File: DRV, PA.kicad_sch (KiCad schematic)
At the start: 157 parts, among them Q10 2SC5171, Q11 2SA1930, Q12 BD139, Q13 BD139, Q14 IRF630, Q15 IRF630, Q16 IRF630, Q17 IRF630, Q2 2N2222A, Q3 2N2222A, Q4 2N3866, Q5 2N3866, Q6 BD139, Q7 BD139, Q8 2SC5171, Q9 2SA1930

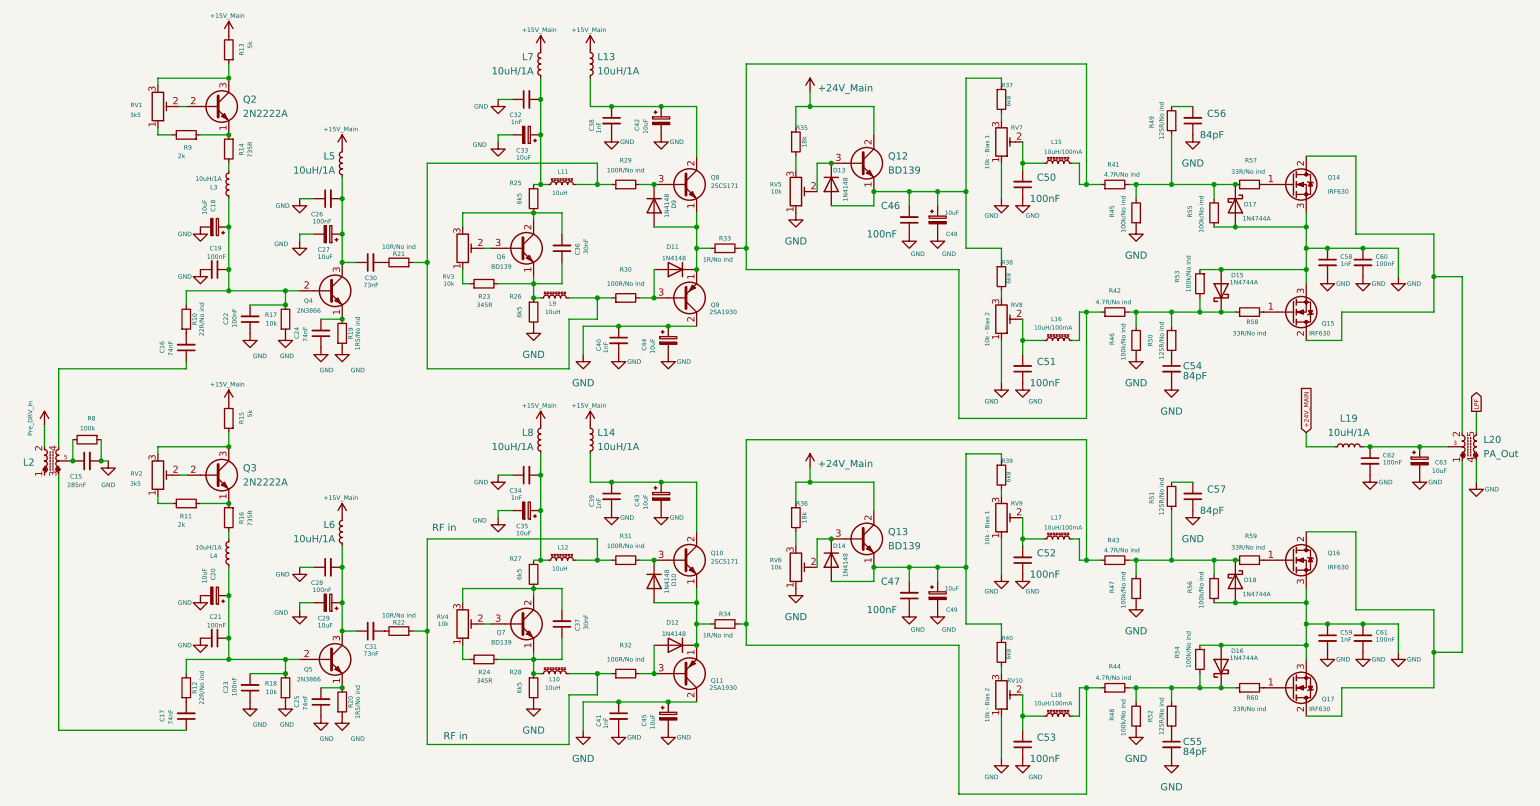
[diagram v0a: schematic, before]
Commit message: Resistive adder of mixers
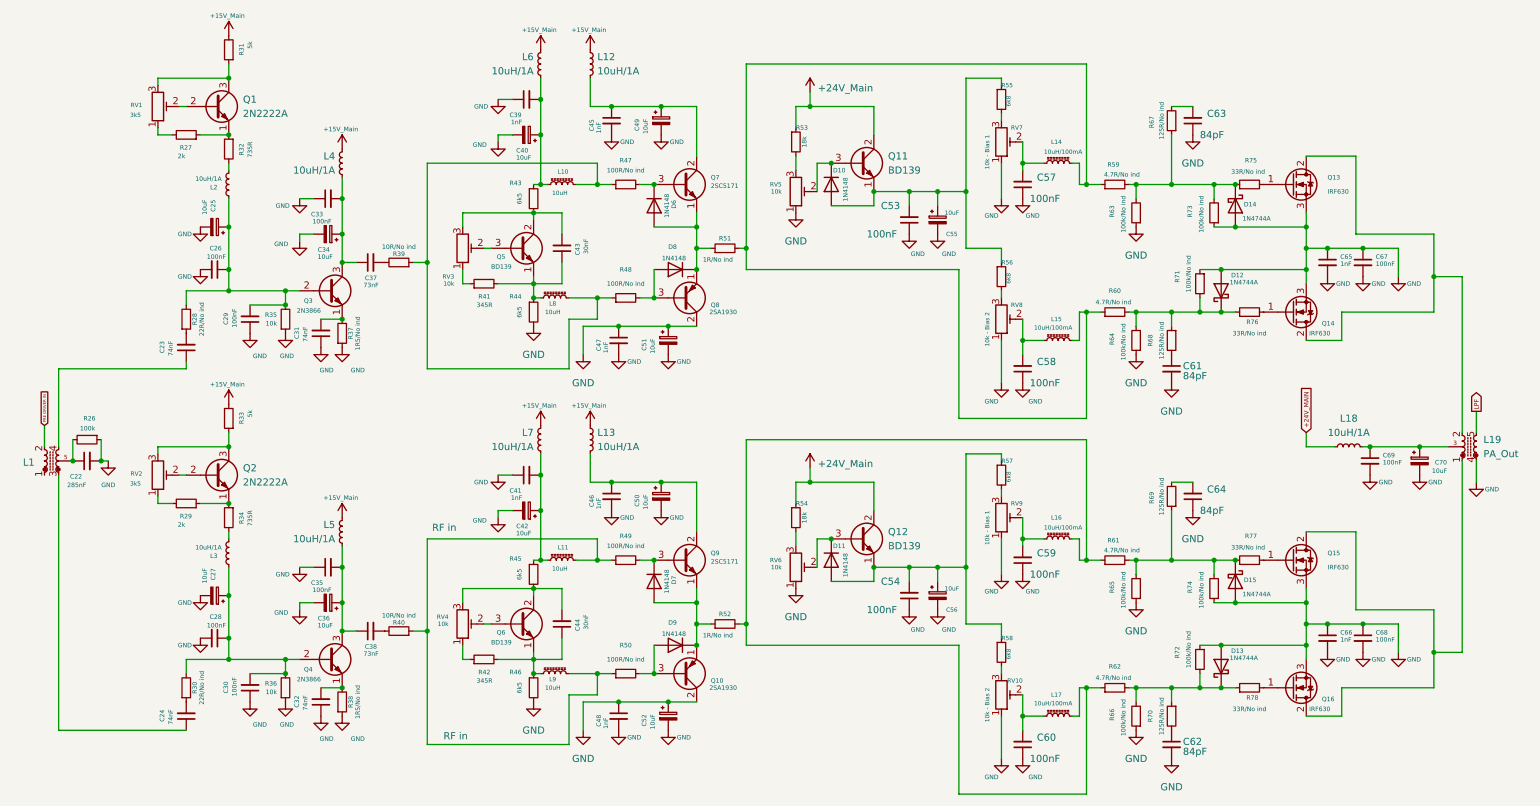
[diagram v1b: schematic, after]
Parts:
- renumbered C15 to C22, C16 to C23, C17 to C24, C18 to C25, C19 to C26, C20 to C27, C21 to C28, C22 to C29, C23 to C30, C24 to C31, C25 to C32, C26 to C33, C27 to C34, C28 to C35, C29 to C36, C30 to C37, C31 to C38, C32 to C39, C33 to C40, C34 to C41, C35 to C42, C36 to C43, C37 to C44, C38 to C45, C39 to C46, C40 to C47, C41 to C48, C42 to C49, C43 to C50, C44 to C51, C45 to C52, C46 to C53, C47 to C54, C48 to C55, C49 to C56, C50 to C57, C51 to C58, C52 to C59, C53 to C60, C54 to C61, C55 to C62, C56 to C63, C57 to C64, C58 to C65, C59 to C66, C60 to C67, C61 to C68, C62 to C69, C63 to C70, D13 to D10, D14 to D11, D15 to D12, D16 to D13, D17 to D14, D18 to D15, D9 to D6, D10 to D7, D11 to D8, D12 to D9, L2 to L1, L11 to L10, L12 to L11, L13 to L12, L14 to L13, L15 to L14, L16 to L15, L17 to L16, L18 to L17, L19 to L18, L20 to L19, L3 to L2, L4 to L3, L5 to L4, L6 to L5, L7 to L6, L8 to L7, L9 to L8, L10 to L9, Q2 to Q1, Q11 to Q10, Q12 to Q11, Q13 to Q12, Q14 to Q13, Q15 to Q14, Q16 to Q15, Q17 to Q16, Q3 to Q2, Q4 to Q3, Q5 to Q4, Q6 to Q5, Q7 to Q6, Q8 to Q7, Q9 to Q8, Q10 to Q9, R8 to R26, R9 to R27, R10 to R28, R11 to R29, R12 to R30, R13 to R31, R14 to R32, R15 to R33, R16 to R34, R17 to R35, R18 to R36, R19 to R37, R20 to R38, R21 to R39, R22 to R40, R23 to R41, R24 to R42, R25 to R43, R26 to R44, R27 to R45, R28 to R46, R29 to R47, R30 to R48, R31 to R49, R32 to R50, R33 to R51, R34 to R52, R35 to R53, R36 to R54, R37 to R55, R38 to R56, R39 to R57, R40 to R58, R41 to R59, R42 to R60, R43 to R61, R44 to R62, R45 to R63, R46 to R64, R47 to R65, R48 to R66, R49 to R67, R50 to R68, R51 to R69, R52 to R70, R53 to R71, R54 to R72, R55 to R73, R56 to R74, R57 to R75, R58 to R76, R59 to R77, R60 to R78
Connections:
- net Pre_DRV_In renamed PRE DRIVER IN

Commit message: BPF Work 2
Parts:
- renumbered C65 to C100, C66 to C101, C67 to C102, C68 to C103, C69 to C104, C70 to C105, C22 to C57, C23 to C58, C24 to C59, C25 to C60, C26 to C61, C27 to C62, C28 to C63, C29 to C64, C30 to C65, C31 to C66, C32 to C67, C33 to C68, C34 to C69, C35 to C70, C36 to C71, C37 to C72, C38 to C73, C39 to C74, C40 to C75, C41 to C76, C42 to C77, C43 to C78, C44 to C79, C45 to C80, C46 to C81, C47 to C82, C48 to C83, C49 to C84, C50 to C85, C51 to C86, C52 to C87, C53 to C88, C54 to C89, C55 to C90, C56 to C91, C57 to C92, C58 to C93, C59 to C94, C60 to C95, C61 to C96, C62 to C97, C63 to C98, C64 to C99, D7 to D10, D8 to D11, D9 to D12, D10 to D13, D11 to D14, D12 to D15, D13 to D16, D14 to D17, D15 to D18, D6 to D9, L1 to L21, L2 to L22, L3 to L23, L4 to L24, L5 to L25, L6 to L26, L7 to L27, L8 to L28, L9 to L29, L10 to L30, L11 to L31, L12 to L32, L13 to L33, L14 to L34, L15 to L35, L16 to L36, L17 to L37, L18 to L38, L19 to L39

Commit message: BPF Work 3
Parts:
- renumbered C72 to C100, C73 to C101, C74 to C102, C75 to C103, C76 to C104, C77 to C105, C78 to C106, C79 to C107, C80 to C108, C81 to C109, C82 to C110, C83 to C111, C84 to C112, C85 to C113, C86 to C114, C87 to C115, C88 to C116, C89 to C117, C90 to C118, C91 to C119, C92 to C120, C93 to C121, C94 to C122, C95 to C123, C96 to C124, C97 to C125, C98 to C126, C99 to C127, C100 to C128, C101 to C129, C102 to C130, C103 to C131, C104 to C132, C105 to C133, C57 to C85, C58 to C86, C59 to C87, C60 to C88, C61 to C89, C62 to C90, C63 to C91, C64 to C92, C65 to C93, C66 to C94, C67 to C95, C68 to C96, C69 to C97, C70 to C98, C71 to C99, L21 to L25, L22 to L26, L23 to L27, L24 to L28, L25 to L29, L26 to L30, L27 to L31, L28 to L32, L29 to L33, L30 to L34, L31 to L35, L32 to L36, L33 to L37, L34 to L38, L35 to L39, L36 to L40, L37 to L41, L38 to L42, L39 to L43, Q1 to Q17, Q2 to Q18, Q3 to Q19, Q4 to Q20, Q5 to Q21, Q6 to Q22, Q7 to Q23, Q8 to Q24, Q9 to Q25, Q10 to Q26, Q11 to Q27, Q12 to Q28, Q13 to Q29, Q14 to Q30, Q15 to Q31, Q16 to Q32, R26 to R34, R27 to R35, R28 to R36, R29 to R37, R30 to R38, R31 to R39, R32 to R40, R33 to R41, R34 to R42, R35 to R43, R36 to R44, R37 to R45, R38 to R46, R39 to R47, R40 to R48, R41 to R49, R42 to R50, R43 to R51, R44 to R52, R45 to R53, R46 to R54, R47 to R55, R48 to R56, R49 to R57, R50 to R58, R51 to R59, R52 to R60, R53 to R61, R54 to R62, R55 to R63, R56 to R64, R57 to R65, R58 to R66, R59 to R67, R60 to R68, R61 to R69, R62 to R70, R63 to R71, R64 to R72, R65 to R73, R66 to R74, R67 to R75, R68 to R76, R69 to R77, R70 to R78, R71 to R79, R72 to R80, R73 to R81, R74 to R82, R75 to R83, R76 to R84, R77 to R85, R78 to R86

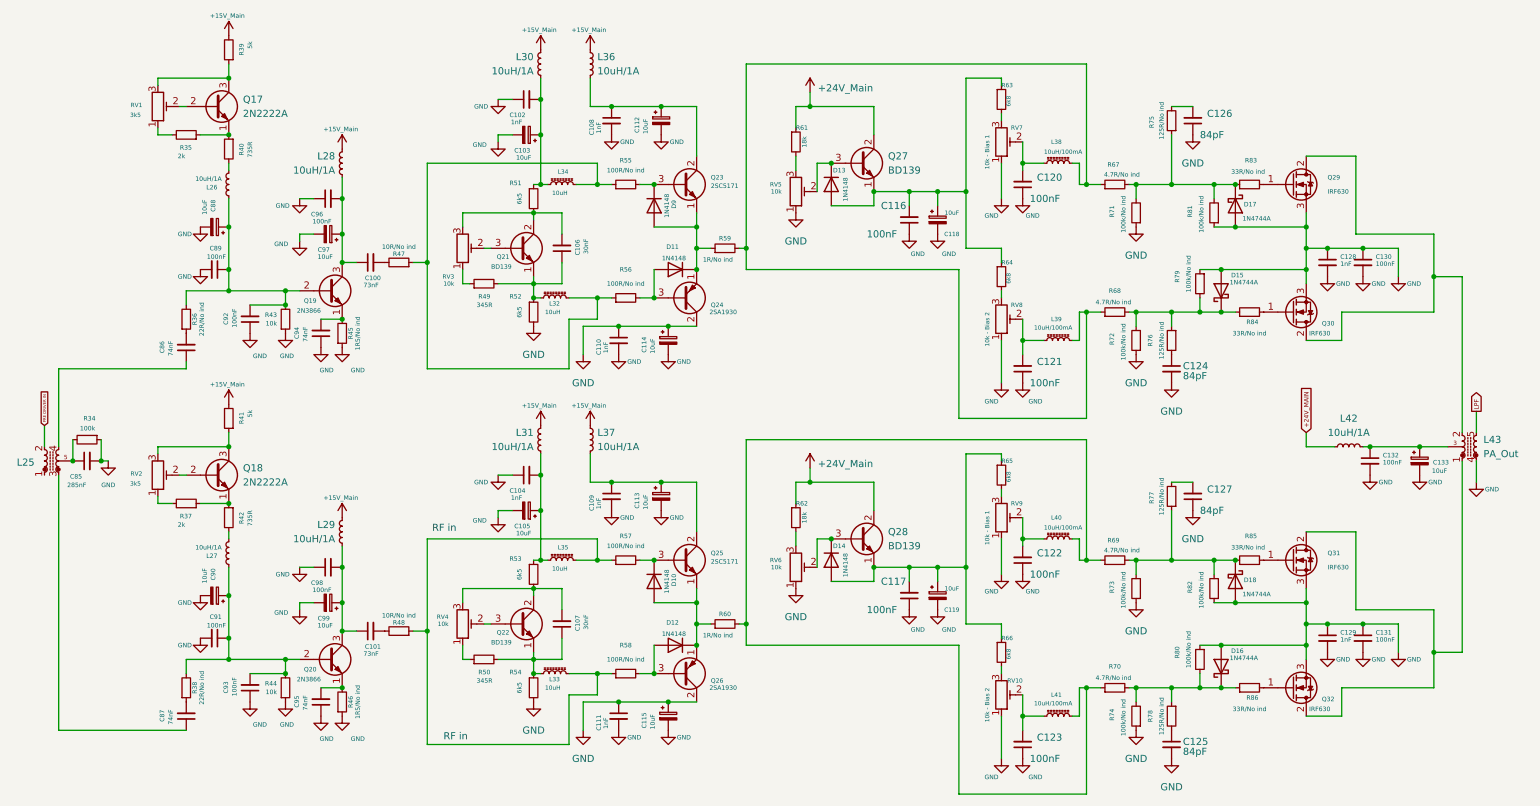
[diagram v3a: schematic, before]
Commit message: Rf RX amplifier, BPF RX
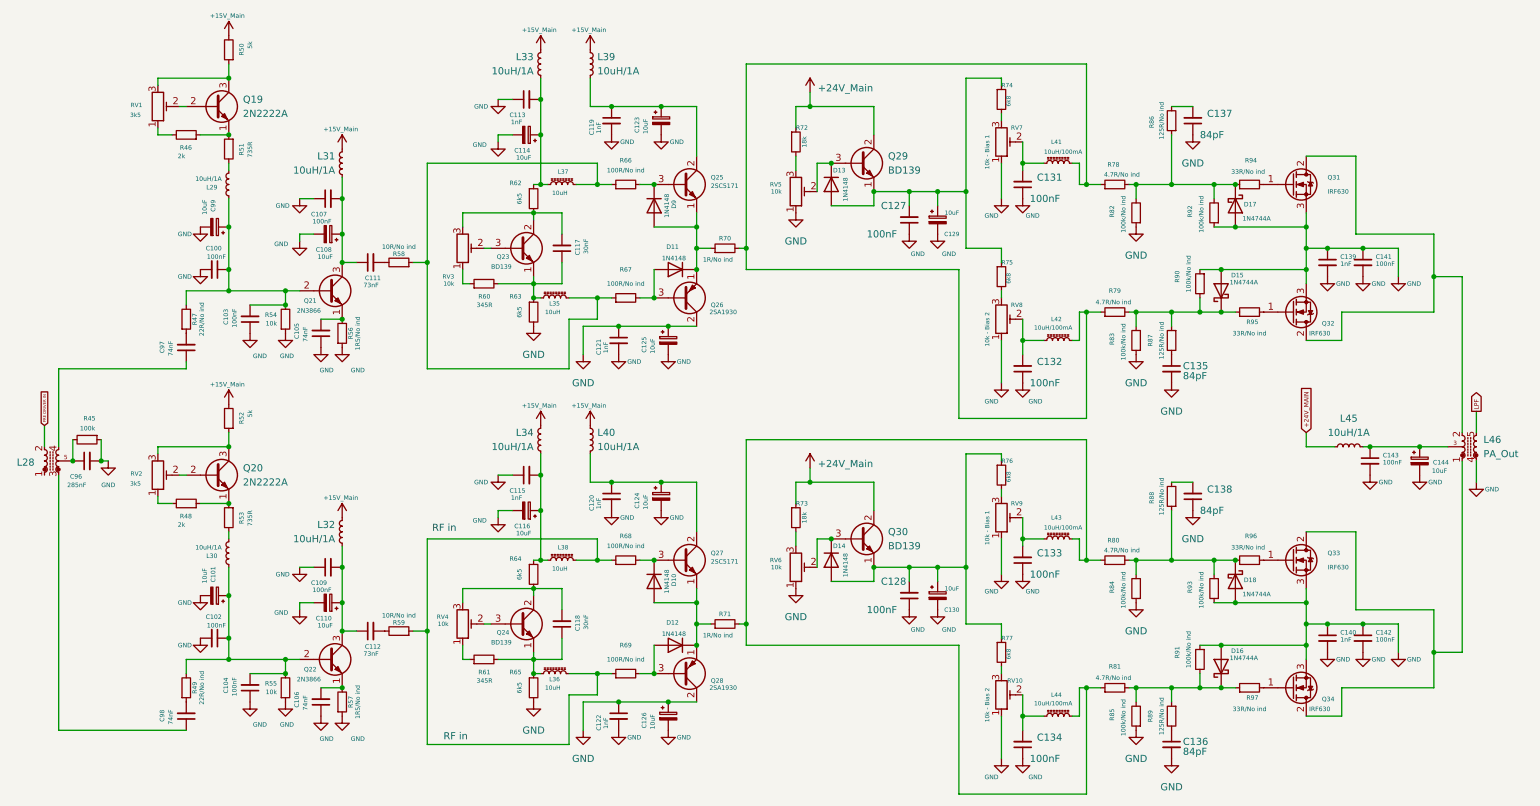
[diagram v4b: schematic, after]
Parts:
- renumbered C89 to C100, C90 to C101, C91 to C102, C92 to C103, C93 to C104, C94 to C105, C95 to C106, C96 to C107, C97 to C108, C98 to C109, C99 to C110, C100 to C111, C101 to C112, C102 to C113, C103 to C114, C104 to C115, C105 to C116, C106 to C117, C107 to C118, C108 to C119, C109 to C120, C110 to C121, C111 to C122, C112 to C123, C113 to C124, C114 to C125, C115 to C126, C116 to C127, C117 to C128, C118 to C129, C119 to C130, C120 to C131, C121 to C132, C122 to C133, C123 to C134, C124 to C135, C125 to C136, C126 to C137, C127 to C138, C128 to C139, C129 to C140, C130 to C141, C131 to C142, C132 to C143, C133 to C144, C85 to C96, C86 to C97, C87 to C98, C88 to C99, L25 to L28, L26 to L29, L27 to L30, L28 to L31, L29 to L32, L30 to L33, L31 to L34, L32 to L35, L33 to L36, L34 to L37, L35 to L38, L36 to L39, L37 to L40, L38 to L41, L39 to L42, L40 to L43, L41 to L44, L42 to L45, L43 to L46, Q17 to Q19, Q18 to Q20, Q19 to Q21, Q20 to Q22, Q21 to Q23, Q22 to Q24, Q23 to Q25, Q24 to Q26, Q25 to Q27, Q26 to Q28, Q27 to Q29, Q28 to Q30, Q29 to Q31, Q30 to Q32, Q31 to Q33, Q32 to Q34, R34 to R45, R35 to R46, R36 to R47, R37 to R48, R38 to R49, R39 to R50, R40 to R51, R41 to R52, R42 to R53, R43 to R54, R44 to R55, R45 to R56, R46 to R57, R47 to R58, R48 to R59, R49 to R60, R50 to R61, R51 to R62, R52 to R63, R53 to R64, R54 to R65, R55 to R66, R56 to R67, R57 to R68, R58 to R69, R59 to R70, R60 to R71, R61 to R72, R62 to R73, R63 to R74, R64 to R75, R65 to R76, R66 to R77, R67 to R78, R68 to R79, R69 to R80, R70 to R81, R71 to R82, R72 to R83, R73 to R84, R74 to R85, R75 to R86, R76 to R87, R77 to R88, R78 to R89, R79 to R90, R80 to R91, R81 to R92, R82 to R93, R83 to R94, R84 to R95, R85 to R96, R86 to R97

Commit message: RF Gain
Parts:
- renumbered C96 to C101, C97 to C102, C98 to C103, C99 to C104, C100 to C105, C101 to C106, C102 to C107, C103 to C108, C104 to C109, C105 to C110, C106 to C111, C107 to C112, C108 to C113, C109 to C114, C110 to C115, C111 to C116, C112 to C117, C113 to C118, C114 to C119, C115 to C120, C116 to C121, C117 to C122, C118 to C123, C119 to C124, C120 to C125, C121 to C126, C122 to C127, C123 to C128, C124 to C129, C125 to C130, C126 to C131, C127 to C132, C128 to C133, C129 to C134, C130 to C135, C131 to C136, C132 to C137, C133 to C138, C134 to C139, C135 to C140, C136 to C141, C137 to C142, C138 to C143, C139 to C144, C140 to C145, C141 to C146, C142 to C147, C143 to C148, C144 to C149, Q19 to Q20, Q20 to Q21, Q21 to Q22, Q22 to Q23, Q23 to Q24, Q24 to Q25, Q25 to Q26, Q26 to Q27, Q27 to Q28, Q28 to Q29, Q29 to Q30, Q30 to Q31, Q31 to Q32, Q32 to Q33, Q33 to Q34, Q34 to Q35, R93 to R100, R94 to R101, R95 to R102, R96 to R103, R97 to R104, R45 to R52, R46 to R53, R47 to R54, R48 to R55, R49 to R56, R50 to R57, R51 to R58, R52 to R59, R53 to R60, R54 to R61, R55 to R62, R56 to R63, R57 to R64, R58 to R65, R59 to R66, R60 to R67, R61 to R68, R62 to R69, R63 to R70, R64 to R71, R65 to R72, R66 to R73, R67 to R74, R68 to R75, R69 to R76, R70 to R77, R71 to R78, R72 to R79, R73 to R80, R74 to R81, R75 to R82, R76 to R83, R77 to R84, R78 to R85, R79 to R86, R80 to R87, R81 to R88, R82 to R89, R83 to R90, R84 to R91, R85 to R92, R86 to R93, R87 to R94, R88 to R95, R89 to R96, R90 to R97, R91 to R98, R92 to R99, RV9 to RV10, RV10 to RV11, RV1 to RV2, RV2 to RV3, RV3 to RV4, RV4 to RV5, RV5 to RV6, RV6 to RV7, RV7 to RV8, RV8 to RV9

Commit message: AGC Work
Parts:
- renumbered Q20 to Q21, Q21 to Q22, Q22 to Q23, Q23 to Q24, Q24 to Q25, Q25 to Q26, Q26 to Q27, Q27 to Q28, Q28 to Q29, Q29 to Q30, Q30 to Q31, Q31 to Q32, Q32 to Q33, Q33 to Q34, Q34 to Q35, Q35 to Q36
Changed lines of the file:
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@@
 		(on_board yes)
 		(dnp no)
-		(property "Reference" "Q28"
+		(property "Reference" "Q29"
 			(at 135.89 111.7599 0)
 			(effects
@@
 			(project "Omega Radio"
 				(path "/3468ce30-82a7-4087-a7ac-02063723d842/24312ef5-36e6-40ee-ad2e-2d0b81e7182c"
-					(reference "Q28")
+					(reference "Q29")
 					(unit 1)
 				)
@@
 		(on_board yes)
 		(dnp no)
-		(property "Reference" "Q25"
+		(property "Reference" "Q26"
 			(at 97.536 125.984 0)
 			(effects
@@
 			(project "Omega Radio"
 				(path "/3468ce30-82a7-4087-a7ac-02063723d842/24312ef5-36e6-40ee-ad2e-2d0b81e7182c"
-					(reference "Q25")
+					(reference "Q26")
 					(unit 1)
 				)
@@
 		(dnp no)
 		(fields_autoplaced yes)
-		(property "Reference" "Q21"
+		(property "Reference" "Q22"
 			(at 52.07 96.5199 0)
 			(effects
@@
 			(project "Omega Radio"
 				(path "/3468ce30-82a7-4087-a7ac-02063723d842/24312ef5-36e6-40ee-ad2e-2d0b81e7182c"
-					(reference "Q21")
+					(reference "Q22")
 					(unit 1)
 				)
@@
 		(on_board yes)
 		(dnp no)
-		(property "Reference" "Q33"
+		(property "Reference" "Q34"
 			(at 245.364 70.612 0)
 			(effects
@@
 			(project "Omega Radio"
 				(path "/3468ce30-82a7-4087-a7ac-02063723d842/24312ef5-36e6-40ee-ad2e-2d0b81e7182c"
-					(reference "Q33")
+					(reference "Q34")
 					(unit 1)
 				)
@@
 		(on_board yes)
 		(dnp no)
-		(property "Reference" "Q23"
+		(property "Reference" "Q24"
 			(at 62.992 132.588 0)
 			(effects
@@
 			(project "Omega Radio"
 				(path "/3468ce30-82a7-4087-a7ac-02063723d842/24312ef5-36e6-40ee-ad2e-2d0b81e7182c"
-					(reference "Q23")
+					(reference "Q24")
 					(unit 1)
 				)
@@
 		(on_board yes)
 		(dnp no)
-		(property "Reference" "Q27"
+		(property "Reference" "Q28"
 			(at 135.89 67.3101 0)
 			(effects
@@
 			(project "Omega Radio"
 				(path "/3468ce30-82a7-4087-a7ac-02063723d842/24312ef5-36e6-40ee-ad2e-2d0b81e7182c"
-					(reference "Q27")
+					(reference "Q28")
 					(unit 1)
 				)
@@
 		(dnp no)
 		(fields_autoplaced yes)
-		(property "Reference" "Q34"
+		(property "Reference" "Q35"
 			(at 246.38 111.7599 0)
 			(effects
@@
 			(project "Omega Radio"
 				(path "/3468ce30-82a7-4087-a7ac-02063723d842/24312ef5-36e6-40ee-ad2e-2d0b81e7182c"
-					(reference "Q34")
+					(reference "Q35")
 					(unit 1)
 				)
@@
 		(on_board yes)
 		(dnp no)
-		(property "Reference" "Q26"
+		(property "Reference" "Q27"
 			(at 135.89 44.4499 0)
 			(effects
@@
 			(project "Omega Radio"
 				(path "/3468ce30-82a7-4087-a7ac-02063723d842/24312ef5-36e6-40ee-ad2e-2d0b81e7182c"
-					(reference "Q26")
+					(reference "Q27")
 					(unit 1)
 				)
@@
 		(dnp no)
 		(fields_autoplaced yes)
-		(property "Reference" "Q30"
+		(property "Reference" "Q31"
 			(at 167.64 40.6399 0)
 			(effects
@@
 			(project "Omega Radio"
 				(path "/3468ce30-82a7-4087-a7ac-02063723d842/24312ef5-36e6-40ee-ad2e-2d0b81e7182c"
-					(reference "Q30")
+					(reference "Q31")
 					(unit 1)
 				)
@@
 		(on_board yes)
 		(dnp no)
-		(property "Reference" "Q22"
+		(property "Reference" "Q23"
 			(at 62.992 66.548 0)
 			(effects
@@
 			(project ""
 				(path "/3468ce30-82a7-4087-a7ac-02063723d842/24312ef5-36e6-40ee-ad2e-2d0b81e7182c"
-					(reference "Q22")
+					(reference "Q23")
 					(unit 1)
 				)
@@
 		(on_board yes)
 		(dnp no)
-		(property "Reference" "Q24"
+		(property "Reference" "Q25"
 			(at 97.536 58.674 0)
 			(effects
@@
 			(project "Omega Radio"
 				(path "/3468ce30-82a7-4087-a7ac-02063723d842/24312ef5-36e6-40ee-ad2e-2d0b81e7182c"
-					(reference "Q24")
+					(reference "Q25")
 					(unit 1)
 				)
@@
 		(dnp no)
 		(fields_autoplaced yes)
-		(property "Reference" "Q31"
+		(property "Reference" "Q32"
 			(at 167.64 107.9499 0)
 			(effects
@@
 			(project "Omega Radio"
 				(path "/3468ce30-82a7-4087-a7ac-02063723d842/24312ef5-36e6-40ee-ad2e-2d0b81e7182c"
-					(reference "Q31")
+					(reference "Q32")
 					(unit 1)
 				)
@@
 		(on_board yes)
 		(dnp no)
-		(property "Reference" "Q29"
+		(property "Reference" "Q30"
 			(at 135.89 134.6201 0)
 			(effects
@@
 			(project "Omega Radio"
 				(path "/3468ce30-82a7-4087-a7ac-02063723d842/24312ef5-36e6-40ee-ad2e-2d0b81e7182c"
-					(reference "Q29")
+					(reference "Q30")
 					(unit 1)
 				)
@@
 		(dnp no)
 		(fields_autoplaced yes)
-		(property "Reference" "Q32"
+		(property "Reference" "Q33"
 			(at 246.38 44.4499 0)
 			(effects
@@
 			(project "Omega Radio"
 				(path "/3468ce30-82a7-4087-a7ac-02063723d842/24312ef5-36e6-40ee-ad2e-2d0b81e7182c"
-					(reference "Q32")
+					(reference "Q33")
 					(unit 1)
 				)
@@
 		(on_board yes)
 		(dnp no)
-		(property "Reference" "Q35"
+		(property "Reference" "Q36"
 			(at 245.364 137.922 0)
 			(effects
@@
 			(project "Omega Radio"
 				(path "/3468ce30-82a7-4087-a7ac-02063723d842/24312ef5-36e6-40ee-ad2e-2d0b81e7182c"
-					(reference "Q35")
+					(reference "Q36")
 					(unit 1)
 				)
@@
 		(dnp no)
 		(fields_autoplaced yes)
-		(property "Reference" "Q20"
+		(property "Reference" "Q21"
 			(at 52.07 30.4799 0)
 			(effects
@@
 			(project ""
 				(path "/3468ce30-82a7-4087-a7ac-02063723d842/24312ef5-36e6-40ee-ad2e-2d0b81e7182c"
-					(reference "Q20")
+					(reference "Q21")
 					(unit 1)
 				)

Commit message: AGC Work 4
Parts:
- renumbered C101 to C105, C102 to C106, C103 to C107, C104 to C108, C105 to C109, C106 to C110, C107 to C111, C108 to C112, C109 to C113, C110 to C114, C111 to C115, C112 to C116, C113 to C117, C114 to C118, C115 to C119, C116 to C120, C117 to C121, C118 to C122, C119 to C123, C120 to C124, C121 to C125, C122 to C126, C123 to C127, C124 to C128, C125 to C129, C126 to C130, C127 to C131, C128 to C132, C129 to C133, C130 to C134, C131 to C135, C132 to C136, C133 to C137, C134 to C138, C135 to C139, C136 to C140, C137 to C141, C138 to C142, C139 to C143, C140 to C144, C141 to C145, C142 to C146, C143 to C147, C144 to C148, C145 to C149, C146 to C150, C147 to C151, C148 to C152, C149 to C153, D9 to D10, D10 to D11, D11 to D12, D12 to D13, D13 to D14, D14 to D15, D15 to D16, D16 to D17, D17 to D18, D18 to D19, R95 to R100, R96 to R101, R97 to R102, R98 to R103, R99 to R104, R100 to R105, R101 to R106, R102 to R107, R103 to R108, R104 to R109, R52 to R57, R53 to R58, R54 to R59, R55 to R60, R56 to R61, R57 to R62, R58 to R63, R59 to R64, R60 to R65, R61 to R66, R62 to R67, R63 to R68, R64 to R69, R65 to R70, R66 to R71, R67 to R72, R68 to R73, R69 to R74, R70 to R75, R71 to R76, R72 to R77, R73 to R78, R74 to R79, R75 to R80, R76 to R81, R77 to R82, R78 to R83, R79 to R84, R80 to R85, R81 to R86, R82 to R87, R83 to R88, R84 to R89, R85 to R90, R86 to R91, R87 to R92, R88 to R93, R89 to R94, R90 to R95, R91 to R96, R92 to R97, R93 to R98, R94 to R99

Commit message: All AGCs done
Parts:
- renumbered C105 to C107, C106 to C108, C107 to C109, C108 to C110, C109 to C111, C110 to C112, C111 to C113, C112 to C114, C113 to C115, C114 to C116, C115 to C117, C116 to C118, C117 to C119, C118 to C120, C119 to C121, C120 to C122, C121 to C123, C122 to C124, C123 to C125, C124 to C126, C125 to C127, C126 to C128, C127 to C129, C128 to C130, C129 to C131, C130 to C132, C131 to C133, C132 to C134, C133 to C135, C134 to C136, C135 to C137, C136 to C138, C137 to C139, C138 to C140, C139 to C141, C140 to C142, C141 to C143, C142 to C144, C143 to C145, C144 to C146, C145 to C147, C146 to C148, C147 to C149, C148 to C150, C149 to C151, C150 to C152, C151 to C153, C152 to C154, C153 to C155, R92 to R100, R93 to R101, R94 to R102, R95 to R103, R96 to R104, R97 to R105, R98 to R106, R99 to R107, R100 to R108, R101 to R109, R102 to R110, R103 to R111, R104 to R112, R105 to R113, R106 to R114, R107 to R115, R108 to R116, R109 to R117, R57 to R65, R58 to R66, R59 to R67, R60 to R68, R61 to R69, R62 to R70, R63 to R71, R64 to R72, R65 to R73, R66 to R74, R67 to R75, R68 to R76, R69 to R77, R70 to R78, R71 to R79, R72 to R80, R73 to R81, R74 to R82, R75 to R83, R76 to R84, R77 to R85, R78 to R86, R79 to R87, R80 to R88, R81 to R89, R82 to R90, R83 to R91, R84 to R92, R85 to R93, R86 to R94, R87 to R95, R88 to R96, R89 to R97, R90 to R98, R91 to R99, RV9 to RV10, RV10 to RV11, RV11 to RV12, RV2 to RV3, RV3 to RV4, RV4 to RV5, RV5 to RV6, RV6 to RV7, RV7 to RV8, RV8 to RV9
